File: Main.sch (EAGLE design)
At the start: 55 parts, among them IC1 LM75A, IC2 ADUM1400, IC3 74LS14N, IC4 MCP2300X/P, Q1 IRF9530, U1 L298, U2 LM 1084 IT5,0, U3 LM 1084 IT3,3, U4 L298, X1 Motors, X3 Battery, X4 Ultra Sonics (5V), X5 ITG-3200, X6 PIRs (5V)

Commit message: 100% route
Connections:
- net N$1 renamed GP0
- net N$12 renamed GP3
- net N$6 renamed GP1
- net N$8 renamed GP2
- removed net N$27: IC4.GP4
- removed net N$28: IC4.GP5
- removed net N$29: IC4.GP6
- removed net N$31: IC4.GP7
- new net GP4: IC4.GP4, R13.1
- new net GP5: IC4.GP5, R12.1
- new net GP6: IC4.GP6, R11.1
- new net GP7: IC4.GP7, R10.1
- net GND: now also IC2.VIA
- net ML_DIR_: no longer IC2.VIA
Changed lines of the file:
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@@
 <class number="0" name="default" width="0.4064" drill="0">
 </class>
-<class number="1" name="10A" width="1.524" drill="0">
+<class number="1" name="10A" width="1.143" drill="0">
 </class>
-<class number="2" name="6A" width="1.016" drill="0">
+<class number="2" name="6A" width="0.889" drill="0">
 </class>
 <class number="3" name="2A" width="0.508" drill="0">
@@
 <part name="GND12" library="supply1" deviceset="GND" device=""/>
 <part name="IC2" library="adum140x" deviceset="ADUM1400" device=""/>
-<part name="GND13" library="supply1" deviceset="GND" device=""/>
 <part name="IC3" library="74xx-eu" deviceset="74*14" device="N" technology="LS" value="74LS14N"/>
 <part name="V1" library="supply" deviceset="VCC" device=""/>
@@
 <instance part="GND12" gate="1" x="-469.9" y="-500.38"/>
 <instance part="IC2" gate="G$1" x="-467.36" y="129.54" rot="R180"/>
-<instance part="GND13" gate="1" x="-487.68" y="99.06"/>
 <instance part="IC3" gate="A" x="-398.78" y="177.8"/>
 <instance part="IC3" gate="B" x="-398.78" y="111.76"/>
@@
 </segment>
 <segment>
-<pinref part="IC2" gate="G$1" pin="GND1@2"/>
-<wire x1="-452.12" y1="139.7" x2="-449.58" y2="139.7" width="0.1524" layer="91"/>
-<wire x1="-449.58" y1="139.7" x2="-449.58" y2="149.86" width="0.1524" layer="91"/>
-<wire x1="-449.58" y1="149.86" x2="-487.68" y2="149.86" width="0.1524" layer="91"/>
-<pinref part="IC2" gate="G$1" pin="GND2@2"/>
-<wire x1="-485.14" y1="139.7" x2="-487.68" y2="139.7" width="0.1524" layer="91"/>
-<wire x1="-487.68" y1="139.7" x2="-487.68" y2="124.46" width="0.1524" layer="91"/>
-<pinref part="GND13" gate="1" pin="GND"/>
-<pinref part="IC2" gate="G$1" pin="GND2@1"/>
-<wire x1="-487.68" y1="124.46" x2="-487.68" y2="101.6" width="0.1524" layer="91"/>
-<wire x1="-485.14" y1="124.46" x2="-487.68" y2="124.46" width="0.1524" layer="91"/>
-<junction x="-487.68" y="124.46"/>
-<wire x1="-487.68" y1="149.86" x2="-487.68" y2="139.7" width="0.1524" layer="91"/>
-<junction x="-487.68" y="139.7"/>
-<pinref part="IC2" gate="G$1" pin="GND1@1"/>
-<wire x1="-452.12" y1="124.46" x2="-449.58" y2="124.46" width="0.1524" layer="91"/>
-<wire x1="-449.58" y1="124.46" x2="-449.58" y2="139.7" width="0.1524" layer="91"/>
-<junction x="-449.58" y="139.7"/>
-</segment>
-<segment>
 <pinref part="C3" gate="G$1" pin="1"/>
 <pinref part="GND10" gate="1" pin="GND"/>
@@
 <wire x1="-459.74" y1="241.3" x2="-464.82" y2="241.3" width="0.1524" layer="91"/>
 <wire x1="-464.82" y1="241.3" x2="-464.82" y2="236.22" width="0.1524" layer="91"/>
+</segment>
+<segment>
+<pinref part="IC2" gate="G$1" pin="GND2@2"/>
+<wire x1="-485.14" y1="139.7" x2="-487.68" y2="139.7" width="0.1524" layer="91"/>
+<label x="-487.68" y="139.7" size="1.778" layer="95"/>
+</segment>
+<segment>
+<pinref part="IC2" gate="G$1" pin="GND2@1"/>
+<wire x1="-485.14" y1="124.46" x2="-487.68" y2="124.46" width="0.1524" layer="91"/>
+<label x="-487.68" y="124.46" size="1.778" layer="95"/>
+</segment>
+<segment>
+<pinref part="IC2" gate="G$1" pin="VIA"/>
+<wire x1="-452.12" y1="127" x2="-439.42" y2="127" width="0.1524" layer="91"/>
+<label x="-439.42" y="127" size="1.778" layer="95"/>
+</segment>
+<segment>
+<pinref part="IC2" gate="G$1" pin="GND1@1"/>
+<wire x1="-452.12" y1="124.46" x2="-449.58" y2="124.46" width="0.1524" layer="91"/>
+<label x="-449.58" y="124.46" size="1.778" layer="95"/>
+</segment>
+<segment>
+<pinref part="IC2" gate="G$1" pin="GND1@2"/>
+<wire x1="-452.12" y1="139.7" x2="-449.58" y2="139.7" width="0.1524" layer="91"/>
+<label x="-449.58" y="139.7" size="1.778" layer="95"/>
 </segment>
 </net>
@@
 <net name="ML_DIR_" class="0">
 <segment>
-<pinref part="IC2" gate="G$1" pin="VIA"/>
-<wire x1="-452.12" y1="127" x2="-439.42" y2="127" width="0.1524" layer="91"/>
-<label x="-439.42" y="127" size="1.778" layer="95"/>
-</segment>
-<segment>
 <pinref part="SV1" gate="G$1" pin="37"/>
 <wire x1="-426.72" y1="533.4" x2="-401.32" y2="533.4" width="0.1524" layer="91"/>
@@
 </segment>
 </net>
-<net name="N$1" class="0">
+<net name="GP0" class="0">
 <segment>
 <pinref part="IC4" gate="G$1" pin="GP0"/>
 <wire x1="-416.56" y1="-251.46" x2="-403.86" y2="-251.46" width="0.1524" layer="91"/>
-</segment>
-</net>
-<net name="N$6" class="0">
+<label x="-403.86" y="-251.46" size="1.778" layer="95"/>
+</segment>
+</net>
+<net name="GP1" class="0">
 <segment>
 <pinref part="IC4" gate="G$1" pin="GP1"/>
 <wire x1="-416.56" y1="-254" x2="-403.86" y2="-254" width="0.1524" layer="91"/>
-</segment>
-</net>
-<net name="N$8" class="0">
+<label x="-403.86" y="-254" size="1.778" layer="95"/>
+</segment>
+</net>
+<net name="GP2" class="0">
 <segment>
 <pinref part="IC4" gate="G$1" pin="GP2"/>
 <wire x1="-416.56" y1="-256.54" x2="-403.86" y2="-256.54" width="0.1524" layer="91"/>
-</segment>
-</net>
-<net name="N$12" class="0">
+<label x="-403.86" y="-256.54" size="1.778" layer="95"/>
+</segment>
+</net>
+<net name="GP3" class="0">
 <segment>
 <pinref part="IC4" gate="G$1" pin="GP3"/>
 <wire x1="-416.56" y1="-259.08" x2="-403.86" y2="-259.08" width="0.1524" layer="91"/>
-</segment>
-</net>
-<net name="N$27" class="0">
+<label x="-403.86" y="-259.08" size="1.778" layer="95"/>
+</segment>
+</net>
+<net name="GP4" class="0">
 <segment>
 <pinref part="IC4" gate="G$1" pin="GP4"/>
 <wire x1="-416.56" y1="-261.62" x2="-403.86" y2="-261.62" width="0.1524" layer="91"/>
-</segment>
-</net>
-<net name="N$28" class="0">
+<label x="-403.86" y="-261.62" size="1.778" layer="95"/>
+</segment>
+<segment>
+<pinref part="R13" gate="G$1" pin="1"/>
+<wire x1="-368.3" y1="-284.48" x2="-378.46" y2="-284.48" width="0.1524" layer="91"/>
+<label x="-378.46" y="-284.48" size="1.778" layer="95"/>
+</segment>
+</net>
+<net name="GP5" class="0">
 <segment>
 <pinref part="IC4" gate="G$1" pin="GP5"/>
 <wire x1="-416.56" y1="-264.16" x2="-403.86" y2="-264.16" width="0.1524" layer="91"/>
-</segment>
-</net>
-<net name="N$29" class="0">
+<label x="-403.86" y="-264.16" size="1.778" layer="95"/>
+</segment>
+<segment>
+<pinref part="R12" gate="G$1" pin="1"/>
+<wire x1="-368.3" y1="-266.7" x2="-378.46" y2="-266.7" width="0.1524" layer="91"/>
+<label x="-378.46" y="-266.7" size="1.778" layer="95"/>
+</segment>
+</net>
+<net name="GP6" class="0">
 <segment>
 <pinref part="IC4" gate="G$1" pin="GP6"/>
 <wire x1="-416.56" y1="-266.7" x2="-403.86" y2="-266.7" width="0.1524" layer="91"/>
-</segment>
-</net>
-<net name="N$31" class="0">
+<label x="-403.86" y="-266.7" size="1.778" layer="95"/>
+</segment>
+<segment>
+<pinref part="R11" gate="G$1" pin="1"/>
+<wire x1="-368.3" y1="-248.92" x2="-378.46" y2="-248.92" width="0.1524" layer="91"/>
+<label x="-378.46" y="-248.92" size="1.778" layer="95"/>
+</segment>
+</net>
+<net name="GP7" class="0">
 <segment>
 <pinref part="IC4" gate="G$1" pin="GP7"/>
 <wire x1="-416.56" y1="-269.24" x2="-403.86" y2="-269.24" width="0.1524" layer="91"/>
-</segment>
-</net>
+<label x="-403.86" y="-269.24" size="1.778" layer="95"/>
+</segment>
+<segment>
+<pinref part="R10" gate="G$1" pin="1"/>
+<wire x1="-368.3" y1="-231.14" x2="-378.46" y2="-231.14" width="0.1524" layer="91"/>
+<label x="-378.46" y="-231.14" size="1.778" layer="95"/>
+</segment>
+</net>

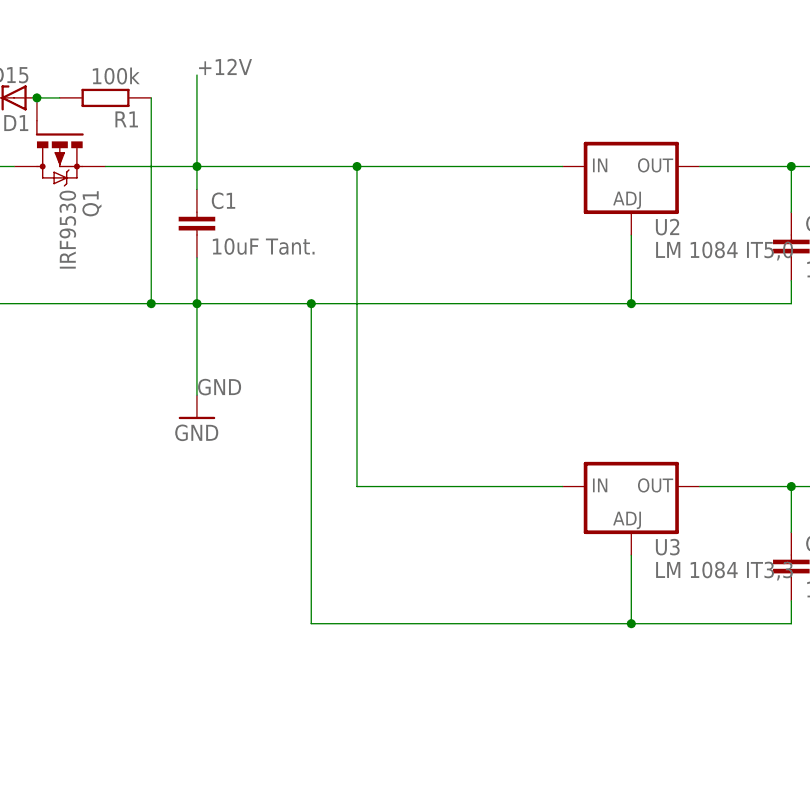
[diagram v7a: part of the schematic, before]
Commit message: placed Cs closer to corresponding parts
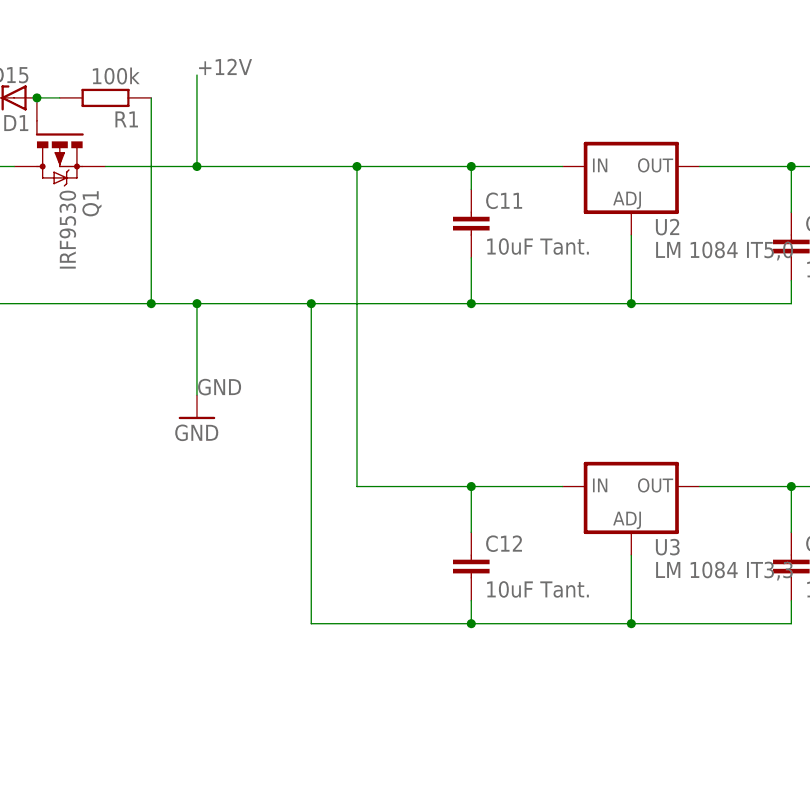
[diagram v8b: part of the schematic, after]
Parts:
- removed C1: 10uF Tant., rcl:C-EU025-040X050
- added C11, C12: 10uF Tant., rcl:C-EU025-040X050
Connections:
- net +12V: now also C11.1, C12.1; no longer C1.1
- net GND: now also C11.2, C12.2; no longer C1.2
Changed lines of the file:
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@@
 <parts>
 <part name="U2" library="v-reg-2" deviceset="LM1084" device="-V" value="LM 1084 IT5,0"/>
-<part name="C1" library="rcl" deviceset="C-EU" device="025-040X050" value="10uF Tant."/>
 <part name="C2" library="rcl" deviceset="C-EU" device="025-040X050" value="10uF Tant."/>
 <part name="U3" library="v-reg-2" deviceset="LM1084" device="-V" value="LM 1084 IT3,3"/>
@@
 <part name="GND20" library="supply1" deviceset="GND" device=""/>
 <part name="IC4" library="adafruit" deviceset="MCP2300X" device="/P"/>
+<part name="C11" library="rcl" deviceset="C-EU" device="025-040X050" value="10uF Tant."/>
+<part name="C12" library="rcl" deviceset="C-EU" device="025-040X050" value="10uF Tant."/>
 </parts>
 <sheets>
@@
 <instances>
 <instance part="U2" gate="G$1" x="-355.6" y="337.82"/>
-<instance part="C1" gate="G$1" x="-403.86" y="332.74"/>
 <instance part="C2" gate="G$1" x="-337.82" y="330.2"/>
 <instance part="U3" gate="G$1" x="-355.6" y="302.26"/>
@@
 <instance part="GND20" gate="1" x="-464.82" y="233.68"/>
 <instance part="IC4" gate="G$1" x="-431.8" y="-261.62"/>
+<instance part="C11" gate="G$1" x="-373.38" y="332.74"/>
+<instance part="C12" gate="G$1" x="-373.38" y="294.64"/>
 </instances>
 <busses>
@@
 <segment>
 <pinref part="U3" gate="G$1" pin="IN"/>
-<wire x1="-363.22" y1="302.26" x2="-386.08" y2="302.26" width="0.1524" layer="91"/>
+<wire x1="-363.22" y1="302.26" x2="-373.38" y2="302.26" width="0.1524" layer="91"/>
 <pinref part="U2" gate="G$1" pin="IN"/>
-<wire x1="-386.08" y1="337.82" x2="-363.22" y2="337.82" width="0.1524" layer="91"/>
+<wire x1="-373.38" y1="302.26" x2="-386.08" y2="302.26" width="0.1524" layer="91"/>
+<wire x1="-386.08" y1="337.82" x2="-373.38" y2="337.82" width="0.1524" layer="91"/>
+<wire x1="-373.38" y1="337.82" x2="-363.22" y2="337.82" width="0.1524" layer="91"/>
 <wire x1="-386.08" y1="302.26" x2="-386.08" y2="337.82" width="0.1524" layer="91"/>
 <junction x="-386.08" y="337.82"/>
@@
 <label x="-403.86" y="347.98" size="1.778" layer="95"/>
 <pinref part="Q1" gate="G$1" pin="S"/>
-<pinref part="C1" gate="G$1" pin="1"/>
-<wire x1="-403.86" y1="335.28" x2="-403.86" y2="337.82" width="0.1524" layer="91"/>
+<pinref part="C11" gate="G$1" pin="1"/>
+<wire x1="-373.38" y1="335.28" x2="-373.38" y2="337.82" width="0.1524" layer="91"/>
+<junction x="-373.38" y="337.82"/>
+<pinref part="C12" gate="G$1" pin="1"/>
+<wire x1="-373.38" y1="297.18" x2="-373.38" y2="302.26" width="0.1524" layer="91"/>
+<junction x="-373.38" y="302.26"/>
 </segment>
 <segment>
@@
 <wire x1="-355.6" y1="330.2" x2="-355.6" y2="322.58" width="0.1524" layer="91"/>
 <junction x="-355.6" y="322.58"/>
-<wire x1="-391.16" y1="322.58" x2="-355.6" y2="322.58" width="0.1524" layer="91"/>
-<wire x1="-355.6" y1="287.02" x2="-391.16" y2="287.02" width="0.1524" layer="91"/>
+<wire x1="-391.16" y1="322.58" x2="-373.38" y2="322.58" width="0.1524" layer="91"/>
+<wire x1="-373.38" y1="322.58" x2="-355.6" y2="322.58" width="0.1524" layer="91"/>
+<wire x1="-355.6" y1="287.02" x2="-373.38" y2="287.02" width="0.1524" layer="91"/>
+<wire x1="-373.38" y1="287.02" x2="-391.16" y2="287.02" width="0.1524" layer="91"/>
 <wire x1="-391.16" y1="287.02" x2="-391.16" y2="322.58" width="0.1524" layer="91"/>
 <junction x="-391.16" y="322.58"/>
@@
 <wire x1="-408.94" y1="345.44" x2="-408.94" y2="322.58" width="0.1524" layer="91"/>
 <junction x="-408.94" y="322.58"/>
-<pinref part="C1" gate="G$1" pin="2"/>
-<wire x1="-403.86" y1="327.66" x2="-403.86" y2="322.58" width="0.1524" layer="91"/>
-</segment>
-<segment>
+<pinref part="C11" gate="G$1" pin="2"/>
+<wire x1="-373.38" y1="327.66" x2="-373.38" y2="322.58" width="0.1524" layer="91"/>
+<junction x="-373.38" y="322.58"/>
+<pinref part="C12" gate="G$1" pin="2"/>
+<wire x1="-373.38" y1="289.56" x2="-373.38" y2="287.02" width="0.1524" layer="91"/>
+<junction x="-373.38" y="287.02"/>
+</segment>
+<segment>
